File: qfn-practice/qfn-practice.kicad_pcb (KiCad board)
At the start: 2 copper layers, 21 x 28 mm, 5 parts, among them IC1 CY8C4245LQI-483, J1 Conn_01x10, J2 Conn_01x10, U1 ATtiny85-20MU, U2 STM32F031G4Ux

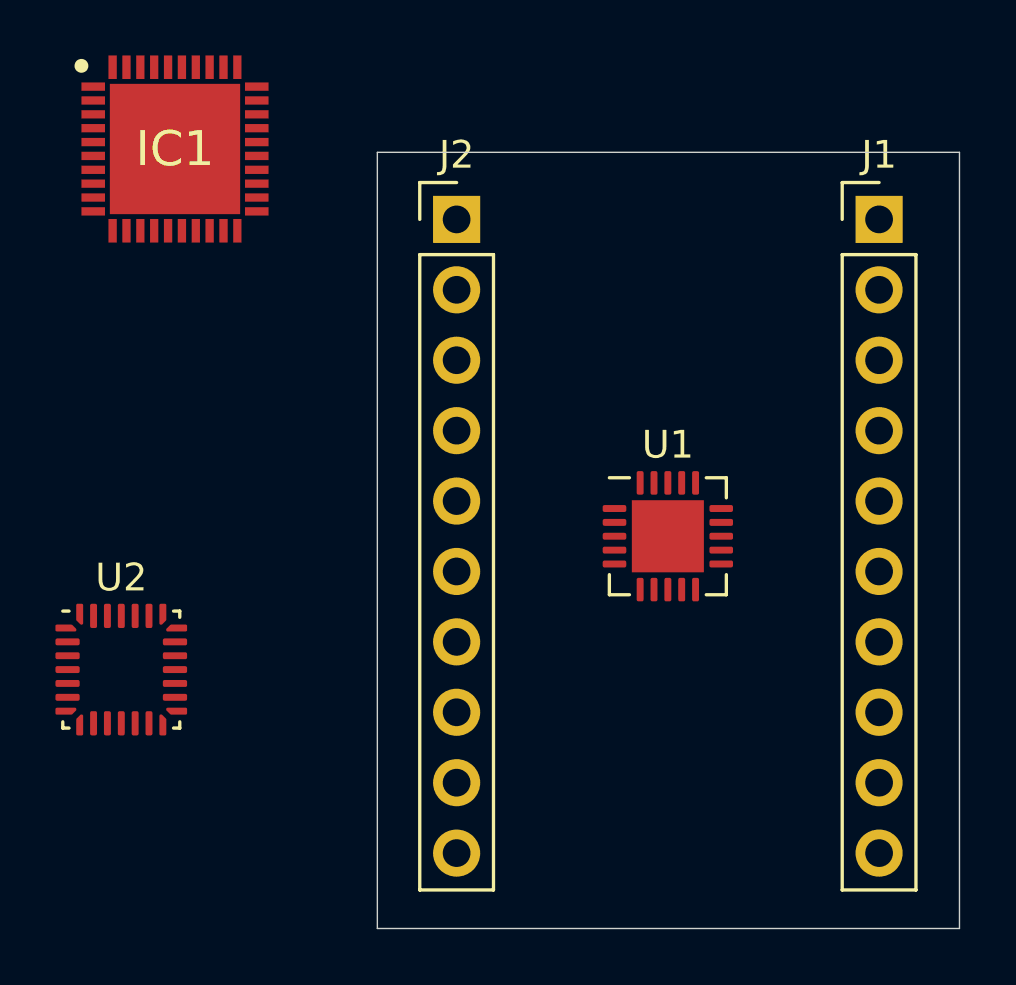
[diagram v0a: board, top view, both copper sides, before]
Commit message: map attiny pins to stm32 footprint
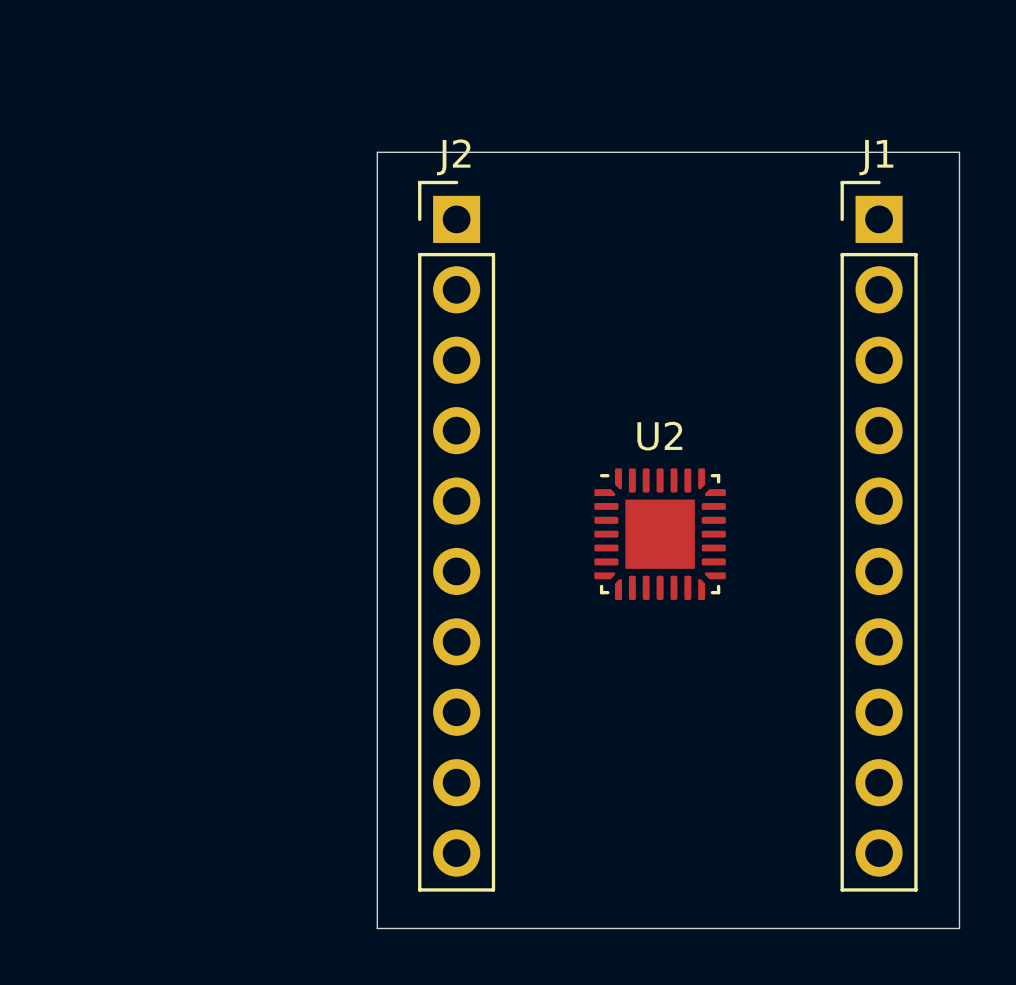
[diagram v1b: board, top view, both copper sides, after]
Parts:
- removed IC1: CY8C4245LQI-483, QFN50P600X600X60-41N-D
- removed U1: ATtiny85-20MU, Package_DFN_QFN:QFN-20-1EP_4x4mm_P0.5mm_EP2.6x2.6mm
- U2: value STM32F031G4Ux -> STM32F031G4Ux-thermal-pad; footprint Package_DFN_QFN:QFN-28_4x4mm_P0.5mm -> SamacSys_Parts:QFN28-4x4mm-0_5mmP-thermalpad
- moved U2 20.0 mm to (157.2, 69.8)
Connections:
- net Net-(U2-Pad11) renamed /AT_GND_ST_PA5
- net Net-(U2-Pad19) renamed /AT_PB2_ST_PA9
- net Net-(U2-Pad2) renamed /AT_PB5_ST_PF0
- net Net-(U2-Pad20) renamed /AT_VCC_ST_PA10
- net Net-(U2-Pad3) renamed /AT_PB3_ST_PF1
- net Net-(U2-Pad6) renamed /AT_PB4_ST_PA0
- U2 pad 16: GND -> /AT_PB0_ST_GND
- U2 pad 17: +3V3 -> /AT_PB1_ST_VDD

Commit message: route to all side pins
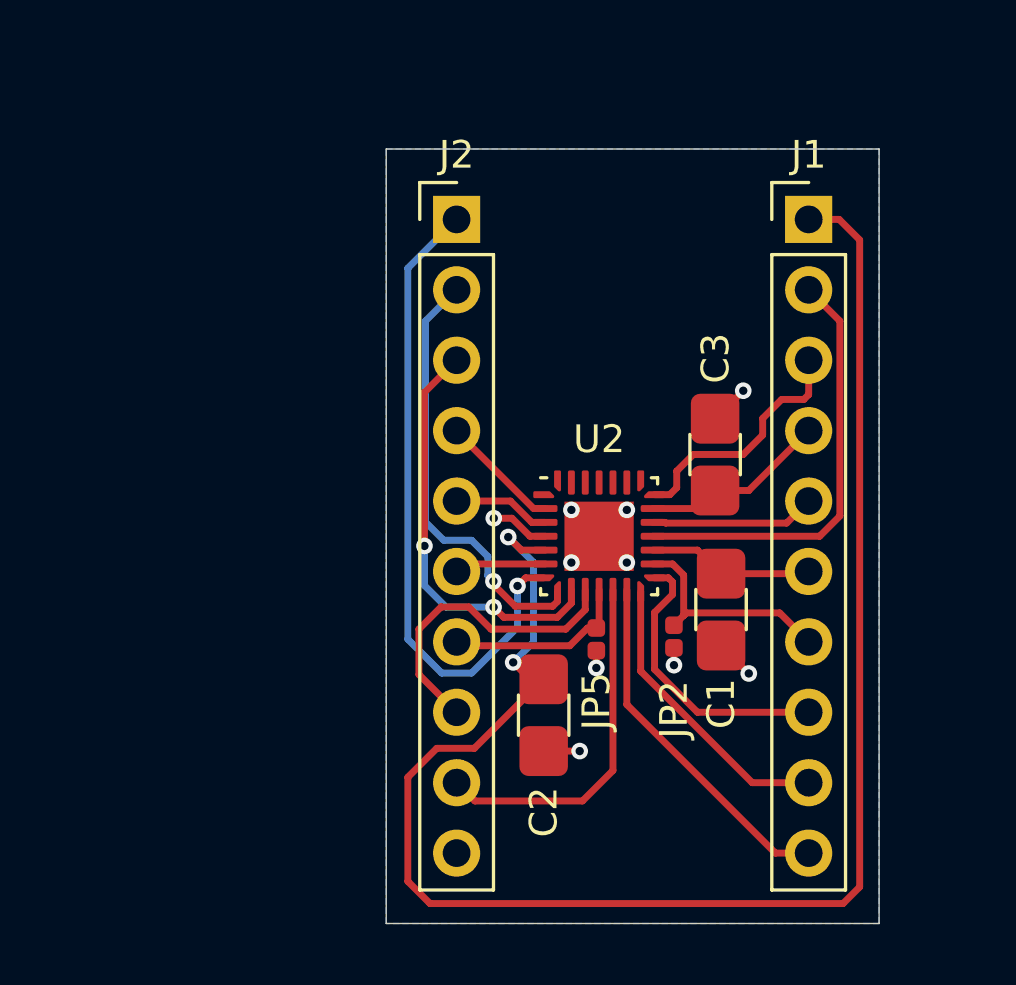
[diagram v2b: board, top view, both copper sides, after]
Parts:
- added C1: 100n, SamacSys_Parts:RC-1206-0805-hybrid, F.Cu at (159.4, 72.5)
- added C2: 100n, SamacSys_Parts:RC-1206-0805-hybrid, F.Cu at (153.0, 76.3)
- added C3: 100n, SamacSys_Parts:RC-1206-0805-hybrid, F.Cu at (159.2, 66.9)
- added JP2: Jumper_NC_Small, SamacSys_Parts:0202-solder-jumper, F.Cu at (157.7, 73.5)
- added JP5: Jumper_NC_Small, SamacSys_Parts:0202-solder-jumper, F.Cu at (154.9, 73.6)
- moved J1 2.54 mm to (162.6, 58.4)
- moved U2 2.20 mm to (155.0, 69.8)
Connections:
- net Net-(U2-Pad1) renamed /ST_BOOT0
- net Net-(U2-Pad22) renamed /ST_USART-TX_SWCLK
- net Net-(U2-Pad23) renamed /ST_USART-RX
- net Net-(U2-Pad24) renamed /ST_PB3_SCK
- net Net-(U2-Pad25) renamed /ST_PB4_MISO
- net Net-(U2-Pad26) renamed /ST_PB5_MOSI
- net Net-(U2-Pad27) renamed /ST_PB6_SCL
- net Net-(U2-Pad28) renamed /ST_PB7_SDA
- net Net-(U2-Pad4) renamed /~ST_RST
- J1 pad 4: /P17 -> /AT_VCC_ST_PA10
- J1 pad 5: /P16 -> /AT_PB2_ST_PA9
- J1 pad 6: /P15 -> /AT_PB1_ST_VDD
- J1 pad 7: /P14 -> /AT_PB0_ST_GND
- J2 pad 4: /P4 -> /AT_PB5_!RESET_ST_PF0
- J2 pad 5: /P5 -> /AT_PB3_ST_PF1
- J2 pad 6: /P6 -> /AT_PB4_ST_PA0
- J2 pad 7: /P7 -> /AT_GND_ST_PA5
- U2 pad 10: Net-(U2-Pad10) -> /P8
- U2 pad 12: Net-(U2-Pad12) -> /P9
- U2 pad 13: Net-(U2-Pad13) -> /P11
- U2 pad 14: Net-(U2-Pad14) -> /P12
- U2 pad 15: Net-(U2-Pad15) -> /P13
- U2 pad 18: Net-(U2-Pad18) -> /P19
- U2 pad 2: /AT_PB5_ST_PF0 -> /AT_PB5_!RESET_ST_PF0
- U2 pad 21: Net-(U2-Pad21) -> /P18
- U2 pad 5: Net-(U2-Pad5) -> +3V3
- U2 pad 7: Net-(U2-Pad7) -> /P1
- U2 pad 8: Net-(U2-Pad8) -> /P2
- U2 pad 9: Net-(U2-Pad9) -> /P3
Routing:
- net +3V3: track 0.00 -> 60.6 mm, vias 0 -> 2
- net /P1: track 0.00 -> 23.6 mm, vias 0 -> 1
- net /P2: track 0.00 -> 15.8 mm, vias 0 -> 1
- net /P19: track 0.00 -> 15.7 mm
- net /P3: track 0.00 -> 15.1 mm, vias 0 -> 2
- net /P11: track 0.00 -> 12.9 mm
- net /P9: track 0.00 -> 12.9 mm
- net /P8: track 0.00 -> 11.2 mm
- net GND: track 0.00 -> 10.9 mm, vias 0 -> 9
- net /P12: track 0.00 -> 10.6 mm
- net /P13: track 0.00 -> 10.3 mm
- net /P18: track 0.00 -> 9.00 mm
- net /AT_PB0_ST_GND: track 0.00 -> 8.21 mm
- net /AT_GND_ST_PA5: track 0.00 -> 7.63 mm
- net /AT_VCC_ST_PA10: track 0.00 -> 6.79 mm
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- added copper zone on B.Cu, net GND
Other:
- board size 21 x 28 mm -> 17.8 x 27.9 mm
- net class Default: via_dia 0.8 -> 0.6; via_drill 0.4 -> 0.3

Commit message: add headers for programming etc
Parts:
- moved JP5 0.06 mm to (154.9, 73.6), turned to 270 degrees
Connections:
- JP5 pad 1: GND -> /AT_GND_ST_PA5
- JP5 pad 2: /AT_GND_ST_PA5 -> GND

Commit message: complete first draft
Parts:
- added J3: Conn_01x03, Connector_PinHeader_2.54mm:PinHeader_1x03_P2.54mm_Vertical, F.Cu at (153.9, 81.3)
- added J4: Conn_01x04, Connector_PinHeader_2.54mm:PinHeader_2x02_P2.54mm_Vertical, F.Cu at (158.9, 61.0)
- added J5: Conn_01x02, Connector_PinHeader_2.54mm:PinHeader_1x02_P2.54mm_Vertical, F.Cu at (156.1, 77.5)
- added J7: Conn_01x03, Connector_PinHeader_2.54mm:PinHeader_1x03_P2.54mm_Vertical, F.Cu at (153.5, 58.4)
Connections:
- U2 pad 12: /P9 -> /ST_PA6
- U2 pad 13: /P11 -> /ST_PA7
- U2 pad 22: /ST_USART-TX_SWCLK -> /ST_USART-TX
- U2 pad 27: /ST_PB6_SCL -> /P1
- U2 pad 28: /ST_PB7_SDA -> /P2
- U2 pad 4: /~ST_RST -> /P3
- U2 pad 7: /P1 -> /P11
- U2 pad 8: /P2 -> /ST_PA2
- U2 pad 9: /P3 -> /P9
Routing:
- net /ST_BOOT0: track 0.00 -> 32.4 mm, vias 0 -> 1
- net /ST_PA2: track 0.00 -> 23.9 mm, vias 0 -> 1
- net /P1: track 23.6 -> 11.2 mm, vias 1 -> 0
- net /P11: track 12.9 -> 24.0 mm, vias 0 -> 2
- net +3V3: track 60.6 -> 50.1 mm
- net /ST_PB3_SCK: track 0.00 -> 10.3 mm
- net /ST_USART-TX: track 0.00 -> 7.86 mm
- net /ST_PB4_MISO: track 0.00 -> 7.62 mm
- net /P2: track 15.8 -> 8.40 mm, vias 1 -> 0
- net /ST_USART-RX: track 0.00 -> 7.08 mm
- net /ST_PA7: track 0.00 -> 6.81 mm
- net /P3: track 15.1 -> 8.39 mm, vias 2 -> 1
- net /ST_PA6: track 0.00 -> 5.97 mm
- net /ST_PB5_MOSI: track 0.00 -> 4.85 mm
- net /~ST_RST: track 2.13 -> 0.00 mm, vias 1 -> 0
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- added copper zone on F.Cu, net GND

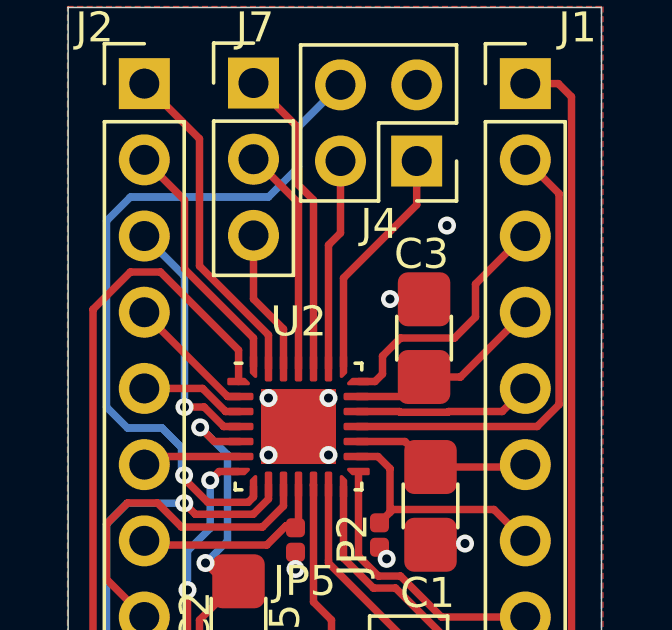
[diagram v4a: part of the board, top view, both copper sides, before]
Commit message: tune track lengths for possible USB pair
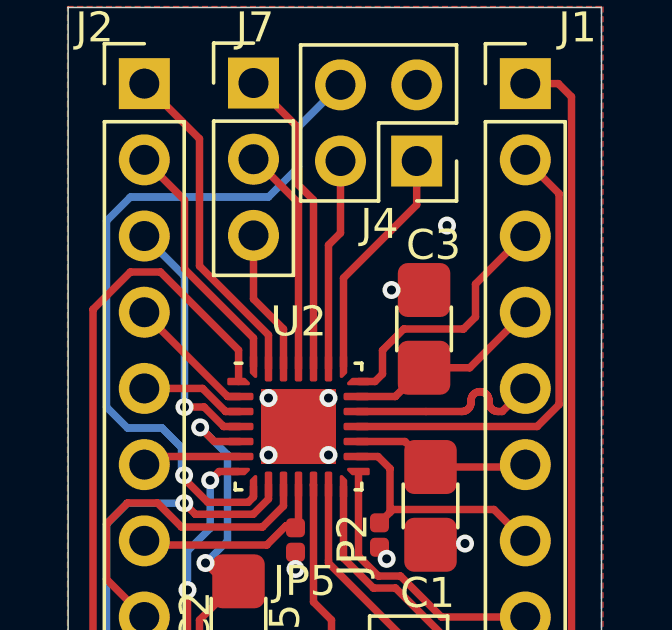
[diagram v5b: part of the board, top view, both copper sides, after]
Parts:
- moved C3 0.31 mm to (159.2, 66.6)
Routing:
- net /AT_PB2_ST_PA9: track 5.96 -> 6.75 mm

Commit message: shuffle things around
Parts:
- J1, J2: moved to B.Cu
- moved C3 0.48 mm to (159.7, 66.7)
- moved C1 0.25 mm to (159.6, 72.5)
- moved JP2 0.20 mm to (157.9, 73.5)
- moved J4 0.20 mm to (158.7, 61.0)
- moved U2 0.20 mm to (155.2, 69.8)
- moved JP5 0.15 mm to (155.1, 73.6)
- moved J7 0.05 mm to (153.6, 58.4)
- turned J1 to 180 degrees
- turned J2 to 180 degrees
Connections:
- J4 pad 4: /ST_PA2 -> /ST_PA1
- U2 pad 10: /P8 -> /P9
- U2 pad 7: /P11 -> /ST_PA1
- U2 pad 8: /ST_PA2 -> /P11
- U2 pad 9: /P9 -> /P8
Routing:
- net /ST_PA2: track 23.9 -> 0.00 mm, vias 1 -> 0
- net /ST_PA1: track 0.00 -> 22.9 mm, vias 0 -> 1
- net /P11: track 24.0 -> 29.2 mm, vias 2 -> 1
- net +3V3: track 50.1 -> 48.0 mm
- net /P9: track 12.7 -> 14.1 mm, vias 1 -> 0
- net GND: track 10.1 -> 11.5 mm, vias 12 -> 15
- net /P13: track 9.22 -> 9.91 mm
- net /ST_BOOT0: track 32.4 -> 32.9 mm, vias 1 -> 0
- net /P8: track 11.1 -> 10.7 mm, vias 0 -> 1
